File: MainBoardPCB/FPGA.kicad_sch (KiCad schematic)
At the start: 26 parts, among them U4 LFE5U-12-TG144, U6 UGA

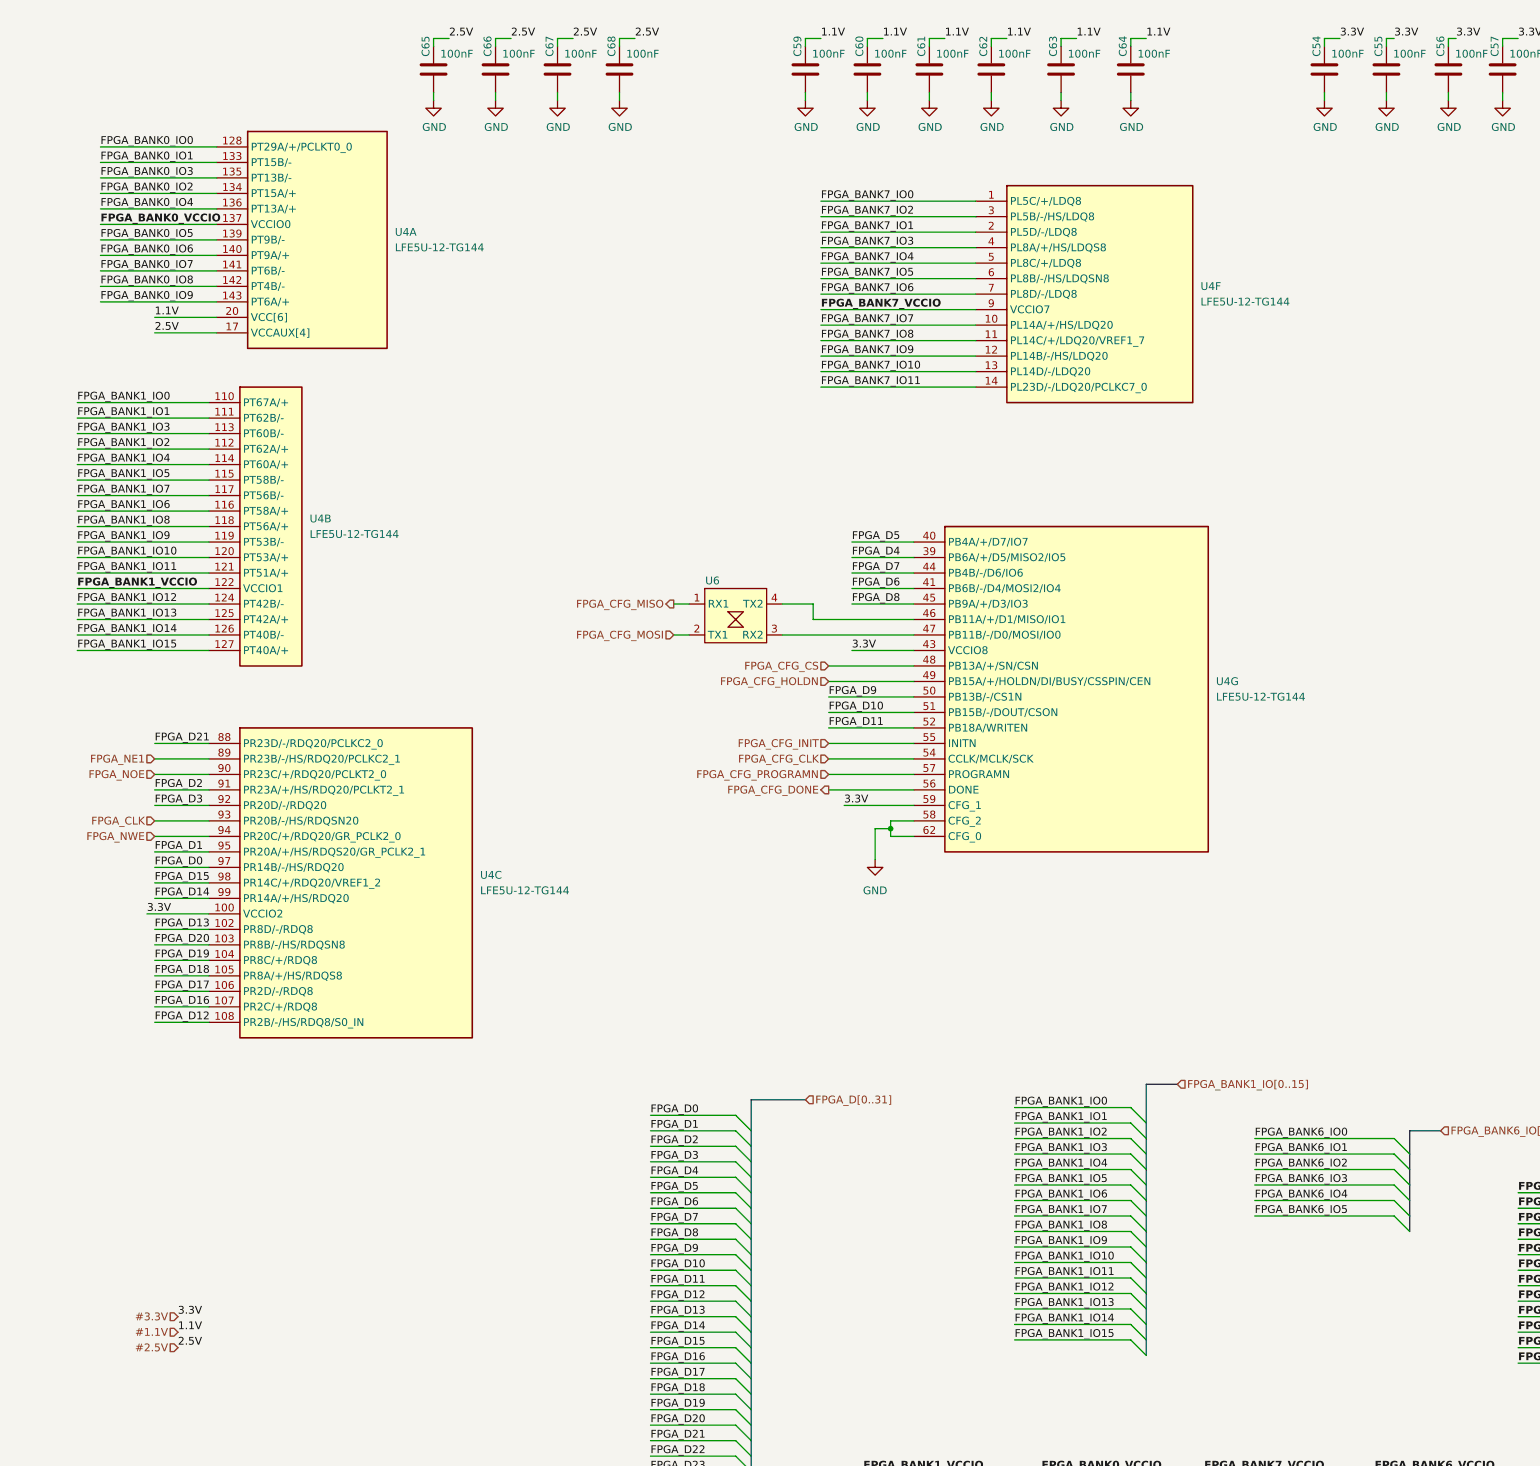
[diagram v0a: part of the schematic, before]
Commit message: Fixes mistake in 1.0, FPGA boot cgf was forced into Master SPI mode
Just make it configurable with pull down resistors.

Signed-off-by: Alexis Jeandet <alexis.jeandet@member.fsf.org>
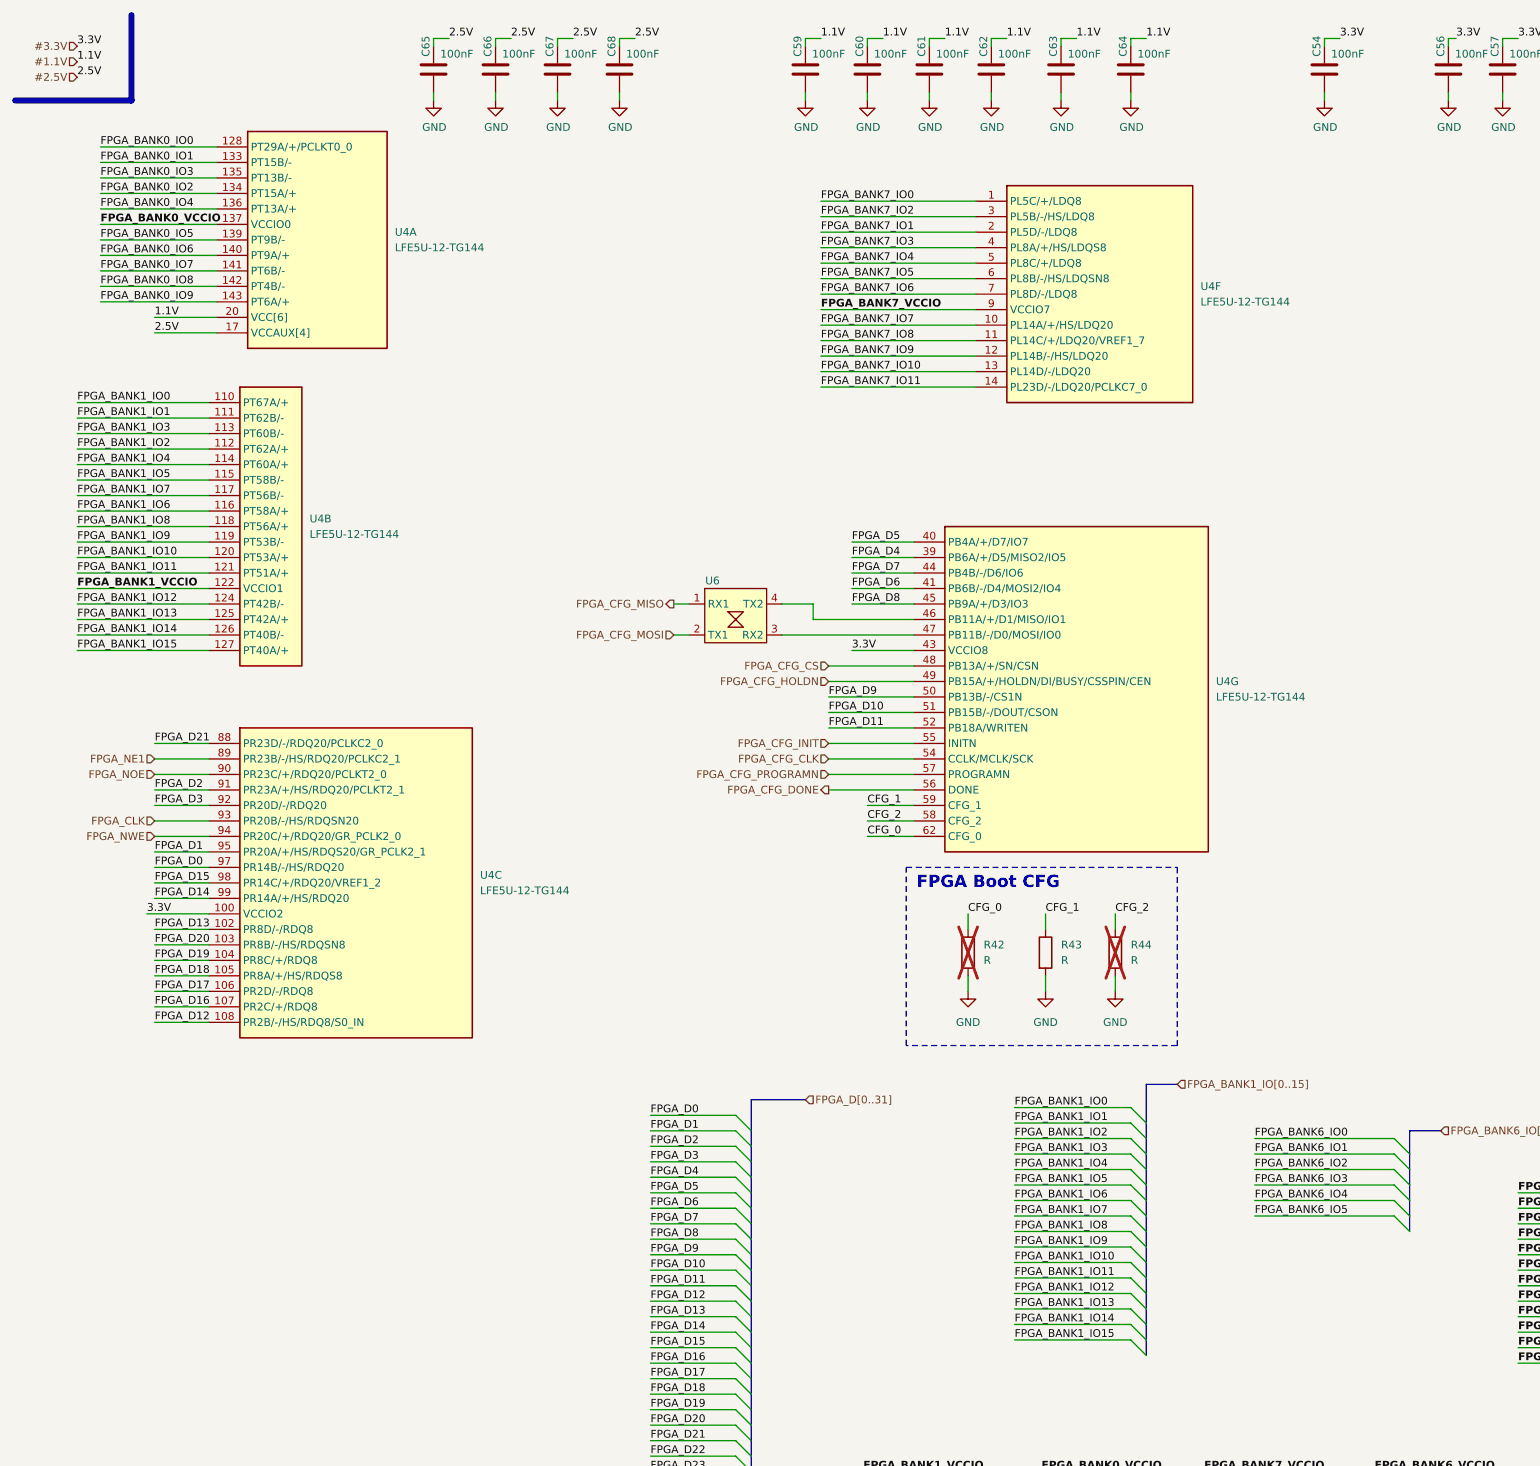
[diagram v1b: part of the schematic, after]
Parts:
- removed C55: 100nF, Capacitor_SMD:C_0402_1005Metric, symbol Device:C
- added R42, R43, R44: R, Resistor_SMD:R_0402_1005Metric_Pad0.72x0.64mm_HandSolder, symbol Device:R
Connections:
- net #3.3V: no longer U4.59 (CFG_1)
- net GND: now also R42.2, R43.2, R44.2; no longer U4.58 (CFG_2), U4.62 (CFG_0)
- new net CFG_0: R42.1, U4.62 (CFG_0)
- new net CFG_1: R43.1, U4.59 (CFG_1)
- new net CFG_2: R44.1, U4.58 (CFG_2)
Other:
- note added: "FPGA Boot CFG"

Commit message: Fixes FPGA CFG slave serial interface wiring
Signed-off-by: Alexis Jeandet <alexis.jeandet@member.fsf.org>
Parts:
- removed U6: UGA, UGA:UGA_0603, symbol UGA:UGA
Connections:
- net FPGA_CFG_HOLDN is gone; now on net FPGA_CFG_MOSI: U4.49 (PB15A/+/HOLDN/DI/BUSY/CSSPIN/CEN)
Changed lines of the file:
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@@
 		)
 	)
-	(wire
-		(pts
-			(xy 138.43 114.3) (xy 160.02 114.3)
-		)
-		(stroke
-			(width 0)
-			(type default)
-		)
-	)
 	(bus
 		(pts
@@
 	(wire
 		(pts
-			(xy 120.65 114.3) (xy 123.19 114.3)
+			(xy 146.05 121.92) (xy 160.02 121.92)
 		)
 		(stroke
@@
 	(wire
 		(pts
-			(xy 143.51 111.76) (xy 160.02 111.76)
-		)
-		(stroke
-			(width 0)
-			(type default)
-		)
-	)
-	(wire
-		(pts
 			(xy 116.84 218.44) (xy 130.81 218.44)
 		)
@@
 	(wire
 		(pts
-			(xy 146.05 121.92) (xy 160.02 121.92)
-		)
-		(stroke
-			(width 0)
-			(type default)
-		)
-	)
-	(wire
-		(pts
 			(xy 195.58 16.51) (xy 198.12 16.51)
 		)
@@
 		)
 	)
-	(wire
-		(pts
-			(xy 143.51 109.22) (xy 143.51 111.76)
-		)
-		(stroke
-			(width 0)
-			(type default)
-		)
-	)
 	(bus
 		(pts
@@
 	(wire
 		(pts
-			(xy 138.43 109.22) (xy 143.51 109.22)
-		)
-		(stroke
-			(width 0)
-			(type default)
-		)
-	)
-	(wire
-		(pts
 			(xy 35.56 157.48) (xy 44.45 157.48)
 		)
@@
 		)
 	)
-	(wire
-		(pts
-			(xy 120.65 109.22) (xy 123.19 109.22)
-		)
-		(stroke
-			(width 0)
-			(type default)
-		)
-	)
 	(bus
 		(pts
@@
 		)
 	)
-	(hierarchical_label "FPGA_CFG_MISO"
-		(shape output)
-		(at 120.65 109.22 180)
-		(fields_autoplaced yes)
-		(effects
-			(font
-				(size 1.27 1.27)
-			)
-			(justify right)
-		)
-	)
 	(hierarchical_label "FPGA_IO2"
 		(shape bidirectional)
@@
 	(hierarchical_label "FPGA_CFG_MOSI"
 		(shape input)
-		(at 120.65 114.3 180)
+		(at 146.05 121.92 180)
 		(fields_autoplaced yes)
 		(effects
@@
 		)
 	)
-	(hierarchical_label "FPGA_CFG_HOLDN"
-		(shape input)
-		(at 146.05 121.92 180)
-		(fields_autoplaced yes)
-		(effects
-			(font
-				(size 1.27 1.27)
-			)
-			(justify right)
-		)
-	)
 	(hierarchical_label "FPGA_IO5"
 		(shape bidirectional)
@@
 					(unit 1)
 				)
-			)
-		)
-	)
-	(symbol
-		(lib_id "UGA:UGA")
-		(at 125.73 115.57 0)
-		(unit 1)
-		(exclude_from_sim no)
-		(in_bom no)
-		(on_board yes)
-		(dnp no)
-		(property "Reference" "U6"
-			(at 127 105.41 0)
-			(effects
-				(font
-					(size 1.27 1.27)
-				)
-			)
-		)
-		(property "Value" "UGA"
-			(at 130.81 103.505 0)
-			(effects
-				(font
-					(size 1.27 1.27)
-				)
-				(hide yes)
-			)
-		)
-		(property "Footprint" "UGA:UGA_0603"
-			(at 125.73 115.57 0)
-			(effects
-				(font
-					(size 1.27 1.27)
-				)
-				(hide yes)
-			)
-		)
-		(property "Datasheet" ""
-			(at 125.73 115.57 0)
-			(effects
-				(font
-					(size 1.27 1.27)
-				)
-				(hide yes)
-			)
-		)
-		(property "Description" ""
-			(at 125.73 115.57 0)
-			(effects
-				(font
-					(size 1.27 1.27)
-				)
-				(hide yes)
-			)
-		)
-		(pin "1"
-		)
-		(pin "2"
-		)
-		(pin "3"
-		)
-		(pin "4"
-		)
-		(instances
-			(project "STicky"
-				(path "/30aa914d-22ff-4c11-8074-f1902c20b00d/00000000-0000-0000-0000-00005f6cbd4c"
-					(reference "U6")
-					(unit 1)
-				)
-			)
-			(project "Fusion"
-				(path "/9f566196-80c5-4736-8658-8706a05587fc/bbe00b15-e65d-4c7a-afa4-5c349809d924"
-					(reference "U8")
-					(unit 1)
-				)

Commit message: New Fusion main board version using a more beefy MCU.
Signed-off-by: Alexis Jeandet <alexis.jeandet@member.fsf.org>
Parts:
- added C1: 100nF, Capacitor_SMD:C_0402_1005Metric, symbol Device:C
- added D301, D302: LED, LED_SMD:LED_0603_1608Metric_Pad1.05x0.95mm_HandSolder, symbol Device:LED
- added R308, R309: 2.2k, Resistor_SMD:R_0402_1005Metric, symbol Device:R
- added X1: ECS-2520MV-xxx-xx, Oscillator:Oscillator_SMD_ECS_2520MV-xxx-xx-4Pin_2.5x2.0mm, symbol Oscillator:ECS-2520MV-xxx-xx
- renumbered C65 to C301, C66 to C302, C67 to C303, C68 to C304, C59 to C305, C60 to C306, C61 to C307, C62 to C308, C5 to C309, C63 to C310, C64 to C311, C31 to C312, C54 to C313, C33 to C314, C56 to C315, C57 to C316, C35 to C317, C58 to C318, C36 to C319, R26 to R301, R27 to R302, R28 to R303, R29 to R304, R42 to R305, R43 to R306, R44 to R307, U4 to U301
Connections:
- net FPGA_D25 is gone; now on net FPGA_D12: U301.80 (PR35C/+/RDQ32)
- net FPGA_D26 is gone; now on net FPGA_D14: U301.78 (PR35D/-/RDQ32)
- net FPGA_D27 is gone; now on net FPGA_D13: U301.79 (PR35B/-/HS/RDQ32/VREF1_3)
- net FPGA_D28 is gone; now on net FPGA_D15: U301.77 (PR41A/+/HS/RDQ44)
- net FPGA_D29 is gone; now on net FPGA_A0: U301.76 (PR41B/-/HS/RDQ44)
- net FPGA_D30 is gone; now on net FPGA_A2: U301.73 (PR41D/-/RDQ44)
- net FPGA_D31 is gone; now on net FPGA_A1: U301.74 (PR41C/+/RDQ44)
- net FPGA_IO0 is gone; now on net FPGA_D8: U301.34 (PL47A/+/HS/LDQ44)
- net FPGA_IO1 is gone; now on net FPGA_HAVE_DATA: U301.33 (PL44D/-/LDQ44)
- net #3.3V: now also C1.1, R308.1, R309.1, X1.1 (Tri-State), X1.4 (VDD)
- net FPGA_A0: no longer U301.72 (PR44C/+/RDQ44)
- net FPGA_A1: no longer U301.71 (PR47A/+/HS/RDQ44)
- net FPGA_A2: no longer U301.69 (PR47C/+/RDQ44/LRC_GPLL0T_IN)
- net FPGA_CLK: now also U301.91 (PR23A/+/HS/RDQ20/PCLKT2_1); no longer U301.93 (PR20B/-/HS/RDQSN20)
- net FPGA_D0: now also U301.50 (PB13B/-/CS1N); no longer U301.97 (PR14B/-/HS/RDQ20)
- net FPGA_D1: now also U301.47 (PB11B/-/D0/MOSI/IO0); no longer U301.95 (PR20A/+/HS/RDQS20/GR_PCLK2_1)
- net FPGA_D10: now also U301.39 (PB6A/+/D5/MISO2/IO5); no longer U301.51 (PB15B/-/DOUT/CSON)
- net FPGA_D11: now also U301.40 (PB4A/+/D7/IO7); no longer U301.52 (PB18A/WRITEN)
- net FPGA_D12: no longer U301.108 (PR2B/-/HS/RDQ8/S0_IN)
- net FPGA_D13: no longer U301.102 (PR8D/-/RDQ8)
- net FPGA_D14: no longer U301.99 (PR14A/+/HS/RDQ20)
- net FPGA_D15: no longer U301.98 (PR14C/+/RDQ20/VREF1_2)
- net FPGA_D2: now also U301.46 (PB11A/+/D1/MISO/IO1); no longer U301.91 (PR23A/+/HS/RDQ20/PCLKT2_1)
- net FPGA_D3: now also U301.45 (PB9A/+/D3/IO3); no longer U301.92 (PR20D/-/RDQ20)
- net FPGA_D4: now also U301.44 (PB4B/-/D6/IO6); no longer U301.39 (PB6A/+/D5/MISO2/IO5)
- net FPGA_D5: now also U301.69 (PR47C/+/RDQ44/LRC_GPLL0T_IN); no longer U301.40 (PB4A/+/D7/IO7)
- net FPGA_D6: now also U301.71 (PR47A/+/HS/RDQ44); no longer U301.41 (PB6B/-/D4/MOSI2/IO4)
- net FPGA_D7: now also U301.72 (PR44C/+/RDQ44); no longer U301.44 (PB4B/-/D6/IO6)
- net FPGA_D8: no longer U301.45 (PB9A/+/D3/IO3)
- net FPGA_D9: now also U301.35 (PL47B/-/HS/LDQ44); no longer U301.50 (PB13B/-/CS1N)
- net FPGA_HAVE_DATA: no longer U301.68 (PR47D/-/RDQ44/LRC_GPLL0C_IN)
- net FPGA_NE1: now also U301.41 (PB6B/-/D4/MOSI2/IO4); no longer U301.89 (PR23B/-/HS/RDQ20/PCLKC2_1)
- net FPGA_NL: now also U301.52 (PB18A/WRITEN); no longer U301.26 (PL41C/+/LDQ44)
- net FPGA_NOE: now also U301.68 (PR47D/-/RDQ44/LRC_GPLL0C_IN); no longer U301.90 (PR23C/+/RDQ20/PCLKT2_0)
- net FPGA_NWAIT: now also U301.51 (PB15B/-/DOUT/CSON); no longer U301.67 (PR47B/-/HS/RDQ44)
- net FPGA_NWE: now also U301.67 (PR47B/-/HS/RDQ44); no longer U301.94 (PR20C/+/RDQ20/GR_PCLK2_0)
- net GND: now also C1.2, X1.2 (GND)
- net FPGA_CFG_CS: no longer names the net of U301.48 (PB13A/+/SN/CSN)
- net FPGA_D16 renamed LED2
- net LED2: now also D302.1 (K)
- net FPGA_D17: no longer names the net of U301.106 (PR2D/-/RDQ8)
- net FPGA_D18 renamed LED1
- net LED1: now also D301.1 (K)
- net FPGA_D19: no longer names the net of U301.104 (PR8C/+/RDQ8)
- net FPGA_D20: no longer names the net of U301.103 (PR8B/-/HS/RDQSN8)
- net FPGA_D21 renamed FPGA_UART2_RX
- net FPGA_D22: no longer names the net of U301.84 (PR32C/+/RDQ32)
- net FPGA_D23 renamed FPGA_UART_RX
- net FPGA_D24 renamed FPGA_UART_TX
- net FPGA_IO2: no longer names the net of U301.31 (PL44C/+/LDQ44)
- net FPGA_IO3: no longer names the net of U301.30 (PL44B/-/HS/LDQSN44)
- net FPGA_IO4: no longer names the net of U301.28 (PL44A/+/HS/LDQS44)
- net FPGA_IO5: no longer names the net of U301.27 (PL41D/-/LDQ44)
- new net: D302.2 (A), R309.2
- new net: D301.2 (A), R308.2
- new net FPGA_OPT_CLK: U301.94 (PR20C/+/RDQ20/GR_PCLK2_0), X1.3 (OUT)
- new net FPGA_UART2_TX: U301.89 (PR23B/-/HS/RDQ20/PCLKC2_1)
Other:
- moved on the sheet: C309, C312, C314, C317, C319
